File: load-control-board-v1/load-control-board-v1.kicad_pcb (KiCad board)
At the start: 4 copper layers, 100 x 80 mm, 94 parts, among them CN1 3511232BMRS0BNA2, CN2 BTC22M4NBB4SCM, CN3 BTC22M4NBB4SCM, Q1 AO3400A, Q2 AO3400A, Q3 IRFP7530PBF, U1 LM317_SOT-223, U10 OPA188xxDBV, U11 OPA188xxDBV, U12 INA186A1IDCKR, U2 74AHC1G04, U22 TL081HIDBVR, U3 LM317_SOT-223, U5 REF5025AD, U6 SN74LVC1G123DCUR_C352969, U7 ALERT_COMP_OUT, U8 OPA188xxDBV

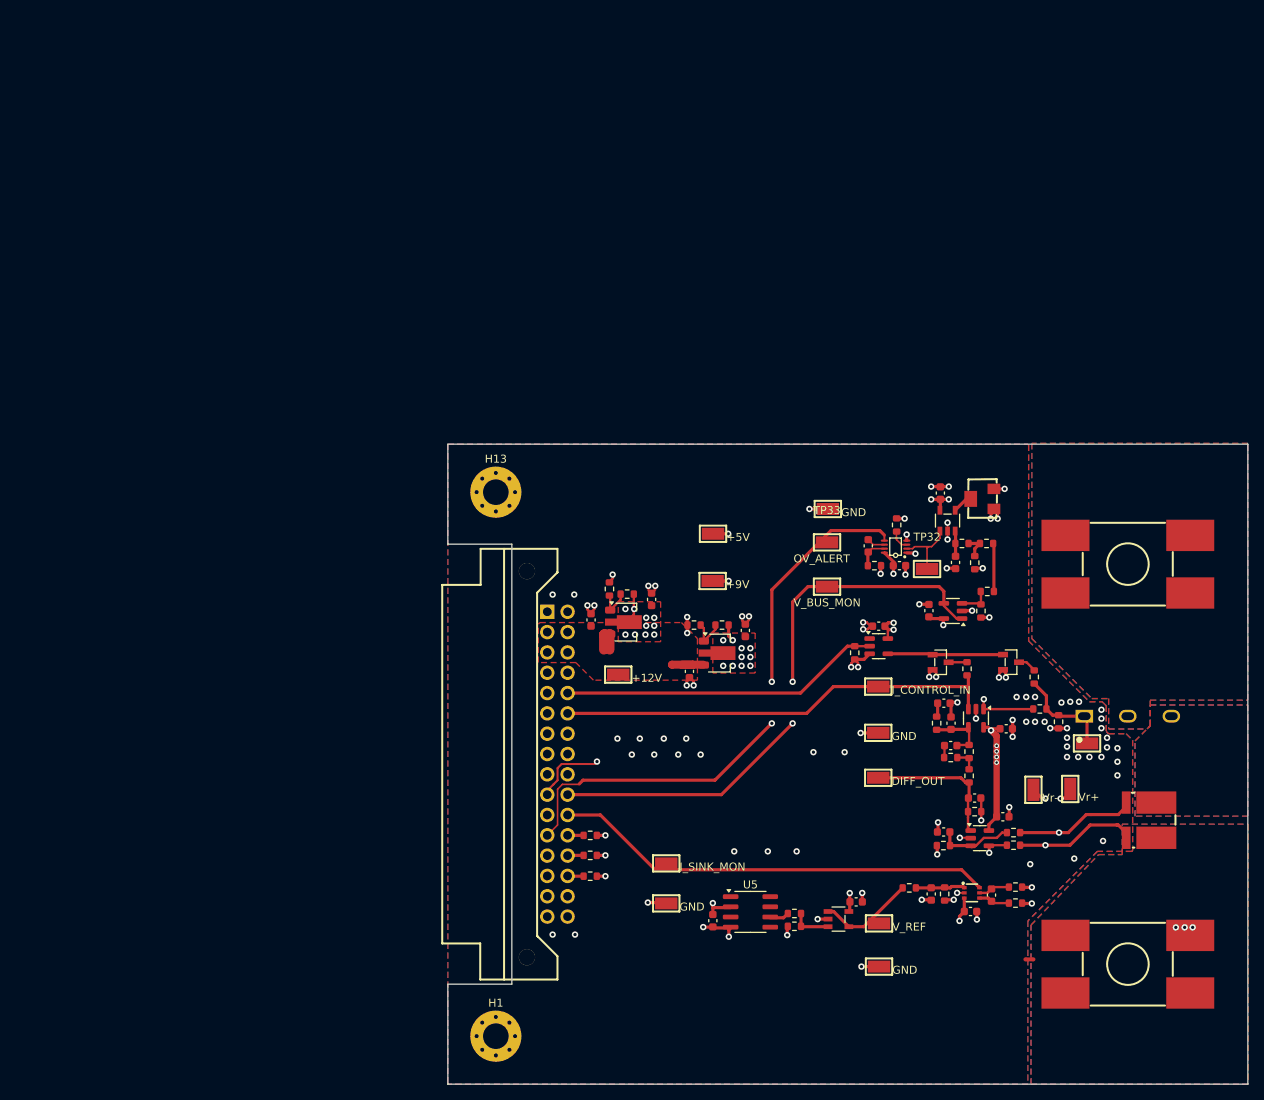
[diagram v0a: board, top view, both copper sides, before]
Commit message: Add design info and logo
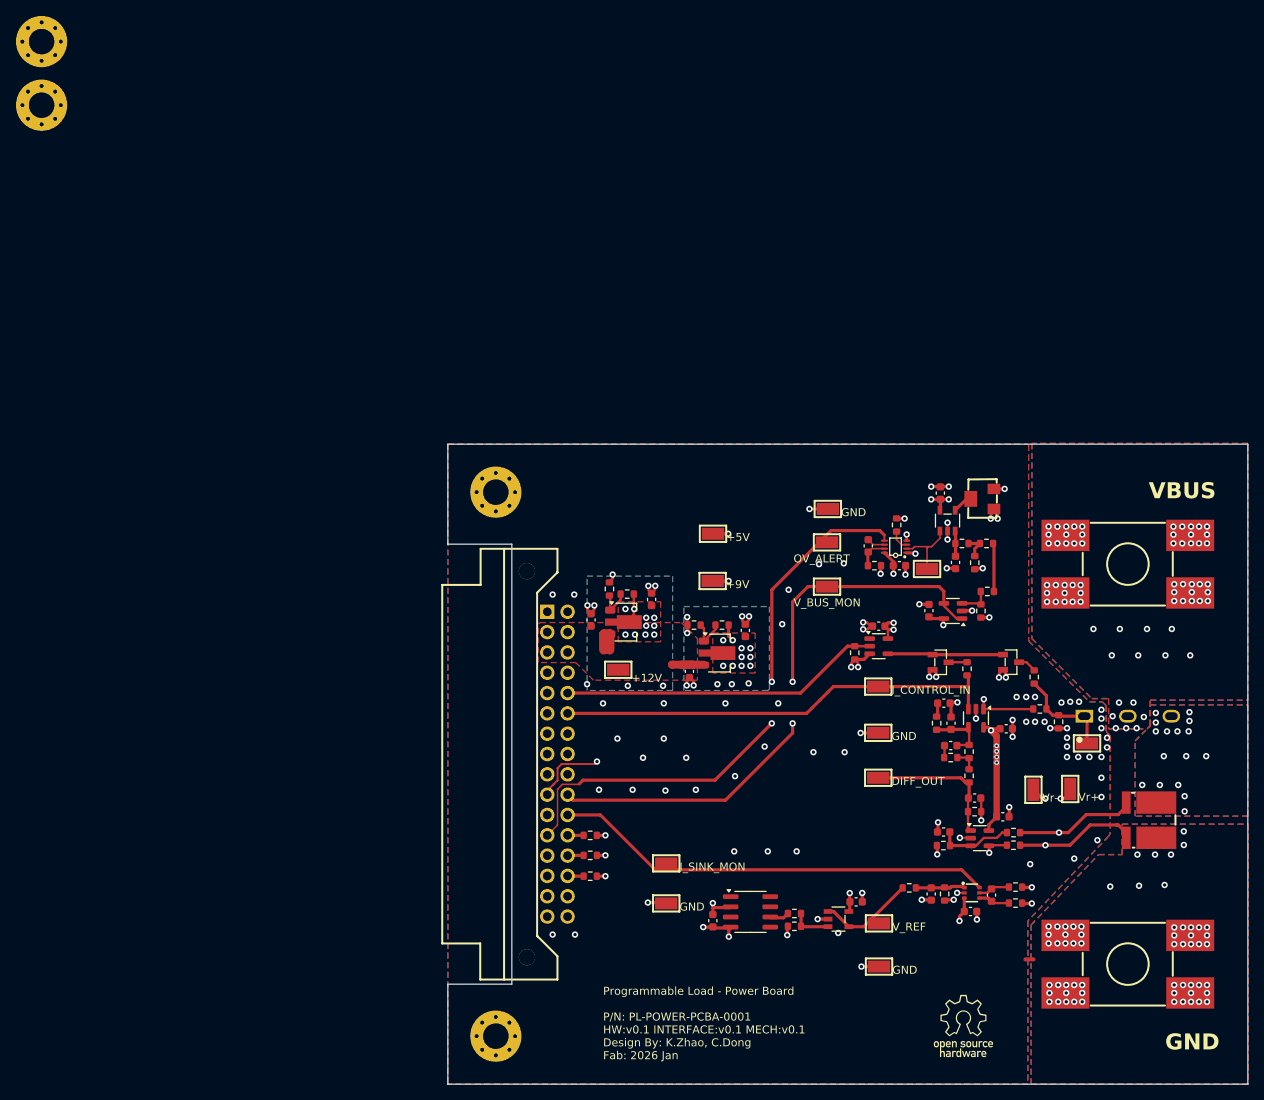
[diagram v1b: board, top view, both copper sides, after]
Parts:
- added H5: MountingHole_Pad, MountingHole:MountingHole_3.2mm_M3_Pad_Via, F.Cu at (3.48, 3.48)
- added H9: MountingHole_Pad, MountingHole:MountingHole_3.2mm_M3_Pad_Via, F.Cu at (3.48, 11.4)
- moved TP1 0.60 mm to (75.6, 82.0)
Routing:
- net Net-(C18-Pad1): track 10.5 -> 13.9 mm
- net +9V: track 70.0 -> 73.2 mm
- net V_BUS_MON: track 71.8 -> 73.1 mm
- net VBUS: vias 0 -> 67
- net Net-(Q3-S): vias 0 -> 16
- net GNDPWR: vias 3 -> 60
- net GND: vias 101 -> 117
- added copper zone on B.Cu, net +5V
- added copper zone on B.Cu, net +9V
- added copper zone on In1.Cu, net GNDPWR
- added copper zone on In2.Cu, net GNDPWR
- added copper zone on In1.Cu, net Net-(Q3-S)
- added copper zone on In2.Cu, net Net-(Q3-S)
- added copper zone on In1.Cu, net VBUS
- added copper zone on In2.Cu, net VBUS
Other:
- board text added: "Programmable Load - Power Board P/N: PL-POWER-PCBA-0001 HW:v0.1 INTERFACE:v0.1 MECH:v0.1 Design By: K.Zhao, C.Dong Fab: 2026 Jan"
- board text added: "VBUS"

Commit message: Correcr INA186A1IDCKR to A2
50V/V is the correct gain
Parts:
- U12: value INA186A1IDCKR -> INA186A2IDCKR

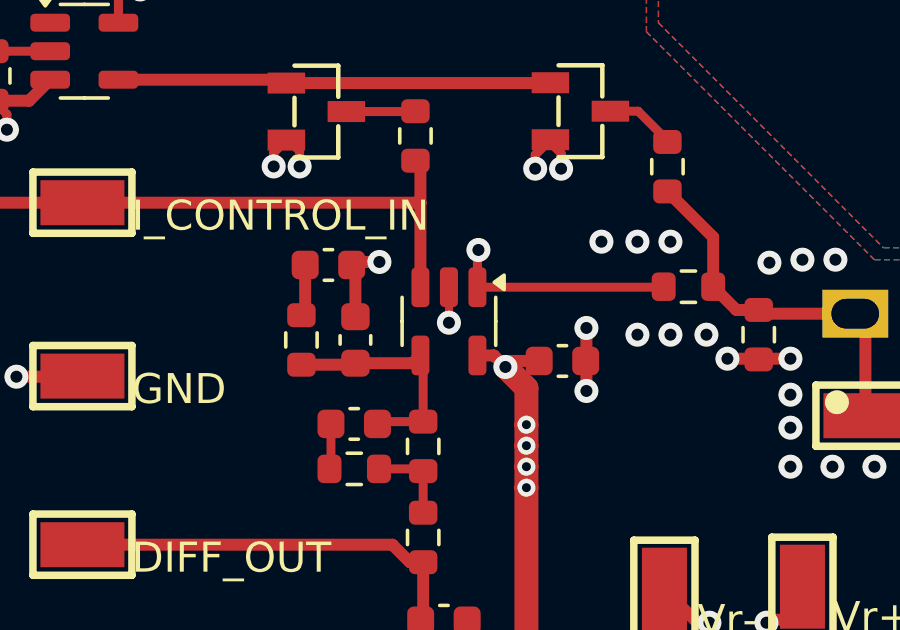
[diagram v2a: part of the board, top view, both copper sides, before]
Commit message: Change INA back to 25V/V, change diff gain to 1:40
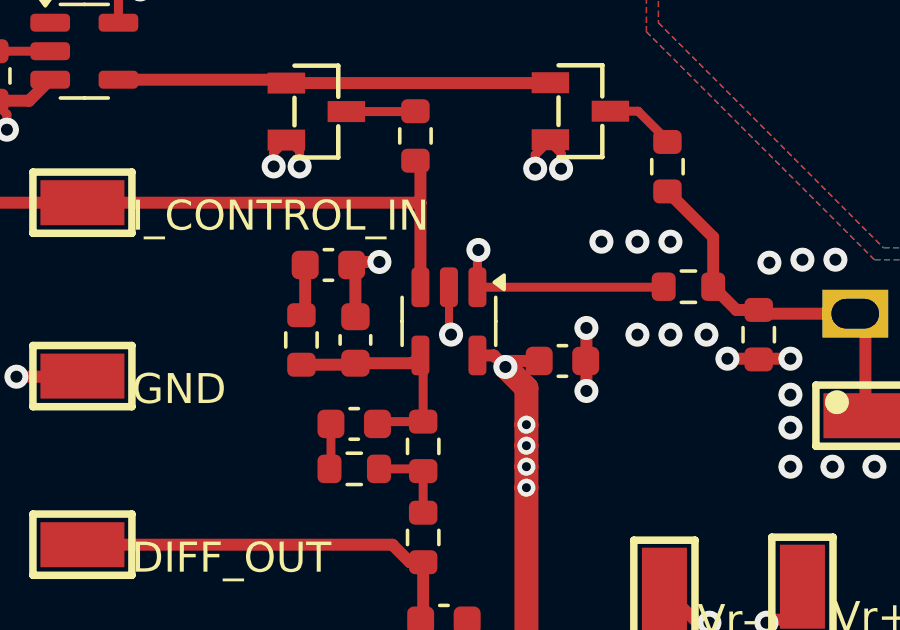
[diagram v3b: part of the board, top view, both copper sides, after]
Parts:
- R16, R20: value 50k -> 40k
- U12: value INA186A2IDCKR -> INA186A1IDCKR
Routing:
- net GND: track 72.9 -> 73.6 mm
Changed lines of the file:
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@@
 	(net 69 "unconnected-(H5-Pad1)")
 	(net 70 "unconnected-(H9-Pad1)_1")
+	(net 71 "unconnected-(H1-Pad1)")
+	(net 72 "unconnected-(H1-Pad1)_1")
+	(net 73 "unconnected-(H1-Pad1)_2")
+	(net 74 "unconnected-(H1-Pad1)_3")
+	(net 75 "unconnected-(H1-Pad1)_5")
+	(net 76 "unconnected-(H1-Pad1)_6")
+	(net 77 "unconnected-(H1-Pad1)_7")
+	(net 78 "unconnected-(H1-Pad1)_8")
+	(net 79 "unconnected-(H5-Pad1)_1")
+	(net 80 "unconnected-(H5-Pad1)_2")
+	(net 81 "unconnected-(H5-Pad1)_3")
+	(net 82 "unconnected-(H5-Pad1)_4")
+	(net 83 "unconnected-(H5-Pad1)_5")
+	(net 84 "unconnected-(H5-Pad1)_6")
+	(net 85 "unconnected-(H5-Pad1)_7")
+	(net 86 "unconnected-(H5-Pad1)_8")
+	(net 87 "unconnected-(H9-Pad1)")
+	(net 88 "unconnected-(H9-Pad1)_2")
+	(net 89 "unconnected-(H9-Pad1)_3")
+	(net 90 "unconnected-(H9-Pad1)_4")
+	(net 91 "unconnected-(H9-Pad1)_5")
+	(net 92 "unconnected-(H9-Pad1)_6")
+	(net 93 "unconnected-(H9-Pad1)_7")
+	(net 94 "unconnected-(H9-Pad1)_8")
+	(net 95 "unconnected-(H13-Pad1)")
+	(net 96 "unconnected-(H13-Pad1)_2")
+	(net 97 "unconnected-(H13-Pad1)_3")
+	(net 98 "unconnected-(H13-Pad1)_4")
+	(net 99 "unconnected-(H13-Pad1)_5")
+	(net 100 "unconnected-(H13-Pad1)_6")
+	(net 101 "unconnected-(H13-Pad1)_7")
+	(net 102 "unconnected-(H13-Pad1)_8")
 	(footprint "Resistor_SMD:R_0603_1608Metric"
 		(layer "F.Cu")
@@
 			)
 		)
-		(property "Value" "50k"
+		(property "Value" "40k"
 			(at -20.175 -0.1606 0)
 			(layer "F.Fab")
@@
 			)
 		)
-		(property "Value" "50k"
+		(property "Value" "40k"
 			(at 16.375 -0.1 0)
 			(layer "F.Fab")
@@
 			(layers "*.Cu" "*.Mask")
 			(remove_unused_layers no)
-			(net 67 "unconnected-(H1-Pad1)_4")
+			(net 75 "unconnected-(H1-Pad1)_5")
 			(pinfunction "1")
 			(pintype "input+no_connect")
@@
 			(layers "*.Cu" "*.Mask")
 			(remove_unused_layers no)
-			(net 67 "unconnected-(H1-Pad1)_4")
+			(net 72 "unconnected-(H1-Pad1)_1")
 			(pinfunction "1")
 			(pintype "input+no_connect")
@@
 			(layers "*.Cu" "*.Mask")
 			(remove_unused_layers no)
-			(net 67 "unconnected-(H1-Pad1)_4")
+			(net 78 "unconnected-(H1-Pad1)_8")
 			(pinfunction "1")
 			(pintype "input+no_connect")
@@
 			(layers "*.Cu" "*.Mask")
 			(remove_unused_layers no)
-			(net 67 "unconnected-(H1-Pad1)_4")
+			(net 74 "unconnected-(H1-Pad1)_3")
 			(pinfunction "1")
 			(pintype "input+no_connect")
@@
 			(layers "*.Cu" "*.Mask")
 			(remove_unused_layers no)
-			(net 67 "unconnected-(H1-Pad1)_4")
+			(net 73 "unconnected-(H1-Pad1)_2")
 			(pinfunction "1")
 			(pintype "input+no_connect")
@@
 			(layers "*.Cu" "*.Mask")
 			(remove_unused_layers no)
-			(net 67 "unconnected-(H1-Pad1)_4")
+			(net 76 "unconnected-(H1-Pad1)_6")
 			(pinfunction "1")
 			(pintype "input+no_connect")
@@
 			(layers "*.Cu" "*.Mask")
 			(remove_unused_layers no)
-			(net 67 "unconnected-(H1-Pad1)_4")
+			(net 77 "unconnected-(H1-Pad1)_7")
 			(pinfunction "1")
 			(pintype "input+no_connect")
@@
 			(layers "*.Cu" "*.Mask")
 			(remove_unused_layers no)
-			(net 67 "unconnected-(H1-Pad1)_4")
+			(net 71 "unconnected-(H1-Pad1)")
 			(pinfunction "1")
 			(pintype "input+no_connect")
@@
 			(layers "*.Cu" "*.Mask")
 			(remove_unused_layers no)
-			(net 69 "unconnected-(H5-Pad1)")
+			(net 79 "unconnected-(H5-Pad1)_1")
 			(pinfunction "1")
 			(pintype "input+no_connect")
@@
 			(layers "*.Cu" "*.Mask")
 			(remove_unused_layers no)
-			(net 69 "unconnected-(H5-Pad1)")
+			(net 82 "unconnected-(H5-Pad1)_4")
 			(pinfunction "1")
 			(pintype "input+no_connect")
@@
 			(layers "*.Cu" "*.Mask")
 			(remove_unused_layers no)
-			(net 69 "unconnected-(H5-Pad1)")
+			(net 81 "unconnected-(H5-Pad1)_3")
 			(pinfunction "1")
 			(pintype "input+no_connect")
@@
 			(layers "*.Cu" "*.Mask")
 			(remove_unused_layers no)
-			(net 69 "unconnected-(H5-Pad1)")
+			(net 83 "unconnected-(H5-Pad1)_5")
 			(pinfunction "1")
 			(pintype "input+no_connect")
@@
 			(layers "*.Cu" "*.Mask")
 			(remove_unused_layers no)
-			(net 69 "unconnected-(H5-Pad1)")
+			(net 80 "unconnected-(H5-Pad1)_2")
 			(pinfunction "1")
 			(pintype "input+no_connect")
@@
 			(layers "*.Cu" "*.Mask")
 			(remove_unused_layers no)
-			(net 69 "unconnected-(H5-Pad1)")
+			(net 86 "unconnected-(H5-Pad1)_8")
 			(pinfunction "1")
 			(pintype "input+no_connect")
@@
 			(layers "*.Cu" "*.Mask")
 			(remove_unused_layers no)
-			(net 69 "unconnected-(H5-Pad1)")
+			(net 84 "unconnected-(H5-Pad1)_6")
 			(pinfunction "1")
 			(pintype "input+no_connect")
@@
 			(layers "*.Cu" "*.Mask")
 			(remove_unused_layers no)
-			(net 69 "unconnected-(H5-Pad1)")
+			(net 85 "unconnected-(H5-Pad1)_7")
 			(pinfunction "1")
 			(pintype "input+no_connect")
@@
 			(layers "*.Cu" "*.Mask")
 			(remove_unused_layers no)
-			(net 70 "unconnected-(H9-Pad1)_1")
+			(net 87 "unconnected-(H9-Pad1)")
 			(pinfunction "1")
 			(pintype "input+no_connect")
@@
 			(layers "*.Cu" "*.Mask")
 			(remove_unused_layers no)
-			(net 70 "unconnected-(H9-Pad1)_1")
+			(net 90 "unconnected-(H9-Pad1)_4")
 			(pinfunction "1")
 			(pintype "input+no_connect")
@@
 			(layers "*.Cu" "*.Mask")
 			(remove_unused_layers no)
-			(net 70 "unconnected-(H9-Pad1)_1")
+			(net 92 "unconnected-(H9-Pad1)_6")
 			(pinfunction "1")
 			(pintype "input+no_connect")
@@
 			(layers "*.Cu" "*.Mask")
 			(remove_unused_layers no)
-			(net 70 "unconnected-(H9-Pad1)_1")
+			(net 88 "unconnected-(H9-Pad1)_2")
 			(pinfunction "1")
 			(pintype "input+no_connect")
@@
 			(layers "*.Cu" "*.Mask")
 			(remove_unused_layers no)
-			(net 70 "unconnected-(H9-Pad1)_1")
+			(net 91 "unconnected-(H9-Pad1)_5")
 			(pinfunction "1")
 			(pintype "input+no_connect")
@@
 			(layers "*.Cu" "*.Mask")
 			(remove_unused_layers no)
-			(net 70 "unconnected-(H9-Pad1)_1")
+			(net 94 "unconnected-(H9-Pad1)_8")
 			(pinfunction "1")
 			(pintype "input+no_connect")
@@
 			(layers "*.Cu" "*.Mask")
 			(remove_unused_layers no)
-			(net 70 "unconnected-(H9-Pad1)_1")
+			(net 89 "unconnected-(H9-Pad1)_3")
 			(pinfunction "1")
 			(pintype "input+no_connect")
@@
 			(layers "*.Cu" "*.Mask")
 			(remove_unused_layers no)
-			(net 70 "unconnected-(H9-Pad1)_1")
+			(net 93 "unconnected-(H9-Pad1)_7")
 			(pinfunction "1")
 			(pintype "input+no_connect")
@@
 			(layers "*.Cu" "*.Mask")
 			(remove_unused_layers no)
-			(net 68 "unconnected-(H13-Pad1)_1")
+			(net 97 "unconnected-(H13-Pad1)_3")
 			(pinfunction "1")
 			(pintype "input+no_connect")
@@
 			(layers "*.Cu" "*.Mask")
 			(remove_unused_layers no)
-			(net 68 "unconnected-(H13-Pad1)_1")
+			(net 95 "unconnected-(H13-Pad1)")
 			(pinfunction "1")
 			(pintype "input+no_connect")
@@
 			(layers "*.Cu" "*.Mask")
 			(remove_unused_layers no)
-			(net 68 "unconnected-(H13-Pad1)_1")
+			(net 96 "unconnected-(H13-Pad1)_2")
 			(pinfunction "1")
 			(pintype "input+no_connect")
@@
 			(layers "*.Cu" "*.Mask")
 			(remove_unused_layers no)
-			(net 68 "unconnected-(H13-Pad1)_1")
+			(net 98 "unconnected-(H13-Pad1)_4")
 			(pinfunction "1")
 			(pintype "input+no_connect")
@@
 			(layers "*.Cu" "*.Mask")
 			(remove_unused_layers no)
-			(net 68 "unconnected-(H13-Pad1)_1")
+			(net 100 "unconnected-(H13-Pad1)_6")
 			(pinfunction "1")
 			(pintype "input+no_connect")
@@
 			(layers "*.Cu" "*.Mask")
 			(remove_unused_layers no)
-			(net 68 "unconnected-(H13-Pad1)_1")
+			(net 101 "unconnected-(H13-Pad1)_7")
 			(pinfunction "1")
 			(pintype "input+no_connect")
@@
 			(layers "*.Cu" "*.Mask")
 			(remove_unused_layers no)
-			(net 68 "unconnected-(H13-Pad1)_1")
+			(net 102 "unconnected-(H13-Pad1)_8")
 			(pinfunction "1")
 			(pintype "input+no_connect")
@@
 			(layers "*.Cu" "*.Mask")
 			(remove_unused_layers no)
-			(net 68 "unconnected-(H13-Pad1)_1")
+			(net 99 "unconnected-(H13-Pad1)_5")
 			(pinfunction "1")
 			(pintype "input+no_connect")
@@
 			)
 		)
-		(property "Value" "INA186A2IDCKR"
+		(property "Value" "INA186A1IDCKR"
 			(at -4.4625 2.425 0)
 			(layer "F.Fab")
@@
 			)
 		)
-		(property "LCSC Part" "C2058238"
+		(property "LCSC Part" "C2058311"
 			(at 0 0 180)
 			(unlocked yes)
@@
 	)
 	(segment
-		(start 120.271 87.576499)
-		(end 120.271 88.0972)
-		(width 0.254)
-		(layer "F.Cu")
-		(net 1)
-	)
-	(segment
 		(start 114.363799 73.808)
 		(end 114.388799 73.833)
@@
 	)
 	(segment
+		(start 120.271 87.576499)
+		(end 120.271 88.422302)
+		(width 0.254)
+		(layer "F.Cu")
+		(net 1)
+	)
+	(segment
+		(start 120.271 88.422302)
+		(end 120.342658 88.49396)
+		(width 0.254)
+		(layer "F.Cu")
+		(net 1)
+	)
+	(segment
 		(start 115.5294 101.0726)
 		(end 115.5294 102.1976)
@@
 	)
 	(segment
+		(start 120.271 88.422302)
+		(end 120.271 86.914)
+		(width 0.254)
+		(layer "F.Cu")
+		(net 1)
+	)
+	(segment
 		(start 91.04 75.8298)
 		(end 91.4448 76.2346)
@@
 	)
 	(segment
-		(start 120.271 88.0972)
-		(end 120.271 86.914)
-		(width 0.254)
-		(layer "F.Cu")
-		(net 1)
-	)
-	(segment
 		(start 105.1169 80.6972)
 		(end 106.2794 80.6972)
@@
 	)
 	(via
-		(at 120.271 88.0972)
+		(at 120.342658 88.49396)
 		(size 0.8)
 		(drill 0.4)
